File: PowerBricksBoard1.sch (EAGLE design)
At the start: 16 parts

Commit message: Revert "Revert "trim""
This reverts commit 46b5d4a1c2a012013371b894087438f3b54206c6.
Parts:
- R5: value 475k -> 510k
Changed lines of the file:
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@@
 <part name="R4" library="SparkFun-Resistors" library_urn="urn:adsk.eagle:library:532" deviceset="RESISTOR" device="0603" package3d_urn="urn:adsk.eagle:package:39650/1" value=" "/>
 <part name="R3" library="SparkFun-Resistors" library_urn="urn:adsk.eagle:library:532" deviceset="RESISTOR" device="0603" package3d_urn="urn:adsk.eagle:package:39650/1" value=" "/>
-<part name="R5" library="SparkFun-Resistors" library_urn="urn:adsk.eagle:library:532" deviceset="RESISTOR" device="0603" package3d_urn="urn:adsk.eagle:package:39650/1" value="475k"/>
+<part name="R5" library="SparkFun-Resistors" library_urn="urn:adsk.eagle:library:532" deviceset="RESISTOR" device="0603" package3d_urn="urn:adsk.eagle:package:39650/1" value="510k"/>
 <part name="U$1" library="Brick_Dist_Connector" deviceset="BRICK2DIST" device=""/>
 </parts>

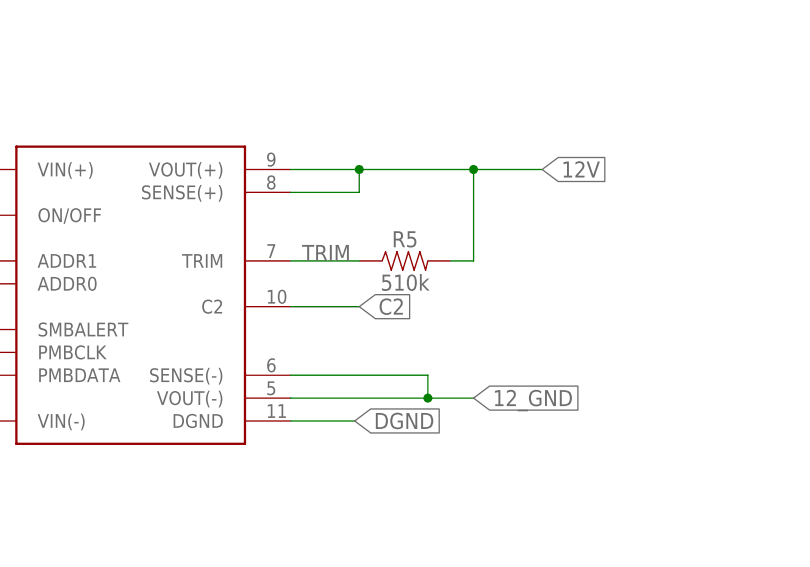
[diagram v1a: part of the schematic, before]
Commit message: Revert "trim"
This reverts commit 0055e3f947d82e2e184832a38c8fbe8e78d74489.
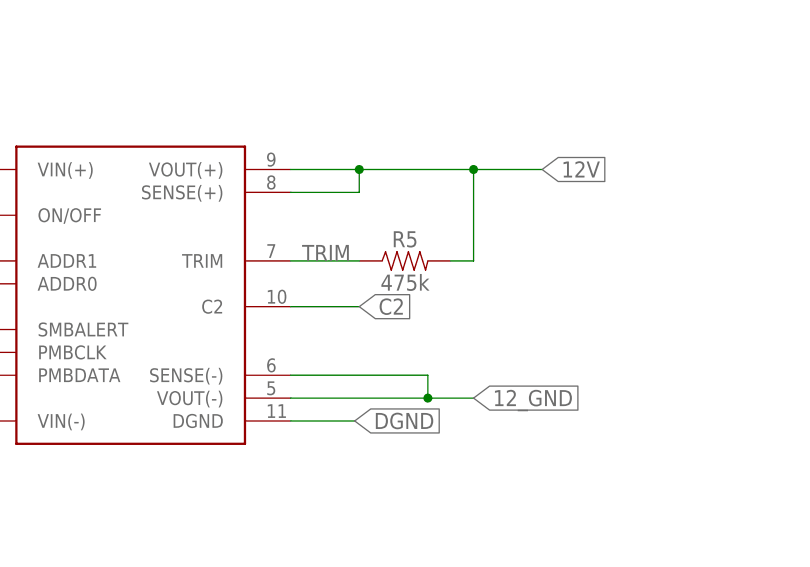
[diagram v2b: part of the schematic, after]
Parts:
- R5: value 510k -> 475k
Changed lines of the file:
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@@
 <part name="R4" library="SparkFun-Resistors" library_urn="urn:adsk.eagle:library:532" deviceset="RESISTOR" device="0603" package3d_urn="urn:adsk.eagle:package:39650/1" value=" "/>
 <part name="R3" library="SparkFun-Resistors" library_urn="urn:adsk.eagle:library:532" deviceset="RESISTOR" device="0603" package3d_urn="urn:adsk.eagle:package:39650/1" value=" "/>
-<part name="R5" library="SparkFun-Resistors" library_urn="urn:adsk.eagle:library:532" deviceset="RESISTOR" device="0603" package3d_urn="urn:adsk.eagle:package:39650/1" value="510k"/>
+<part name="R5" library="SparkFun-Resistors" library_urn="urn:adsk.eagle:library:532" deviceset="RESISTOR" device="0603" package3d_urn="urn:adsk.eagle:package:39650/1" value="475k"/>
 <part name="U$1" library="Brick_Dist_Connector" deviceset="BRICK2DIST" device=""/>
 </parts>
